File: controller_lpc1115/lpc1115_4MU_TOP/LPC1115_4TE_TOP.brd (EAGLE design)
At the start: 67 x 40.8 mm, 102 parts, among them P2 ISP, Q1 BC856, Q2 BCP52, Q3 BC847C, U1 LPC1115FBD48, U2 BD9G101, U3 XO32 12MHz

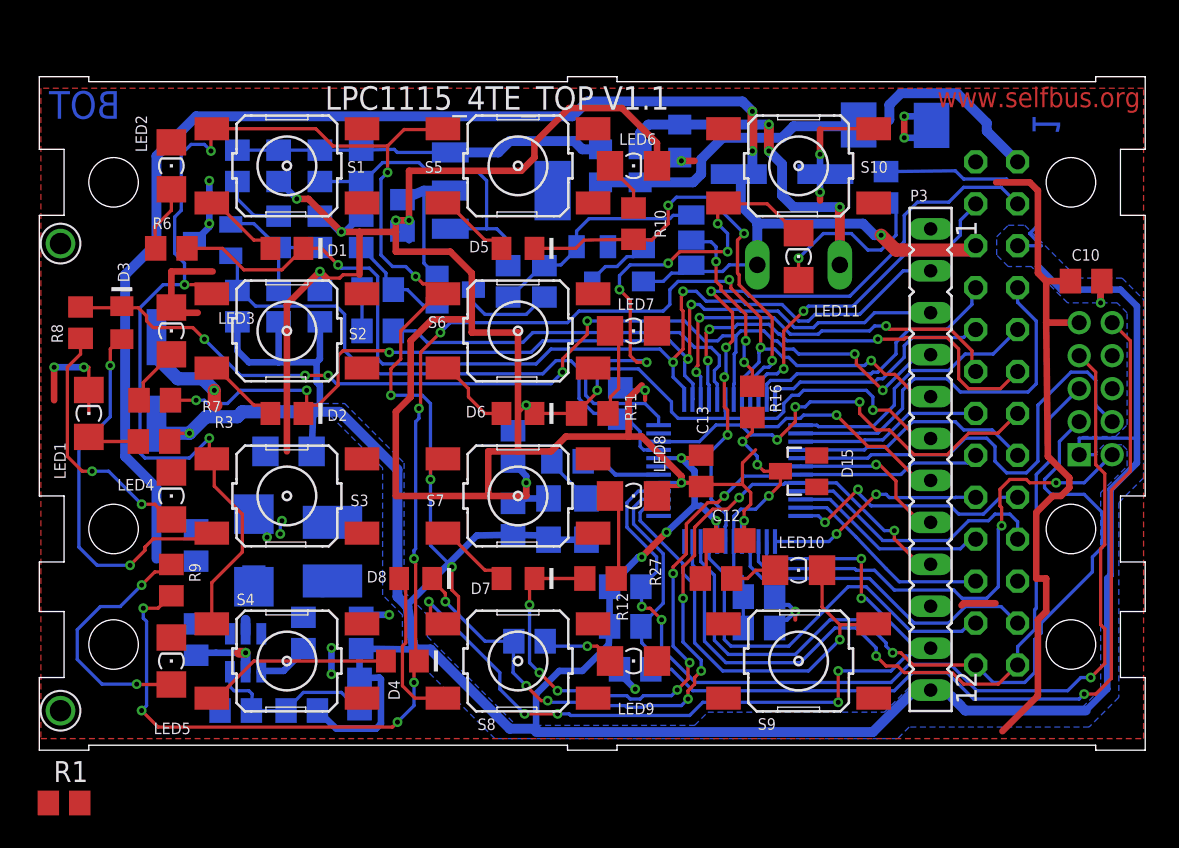
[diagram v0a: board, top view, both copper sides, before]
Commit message: [ctrl_4MU_TOP] - intermediate status of re-routing
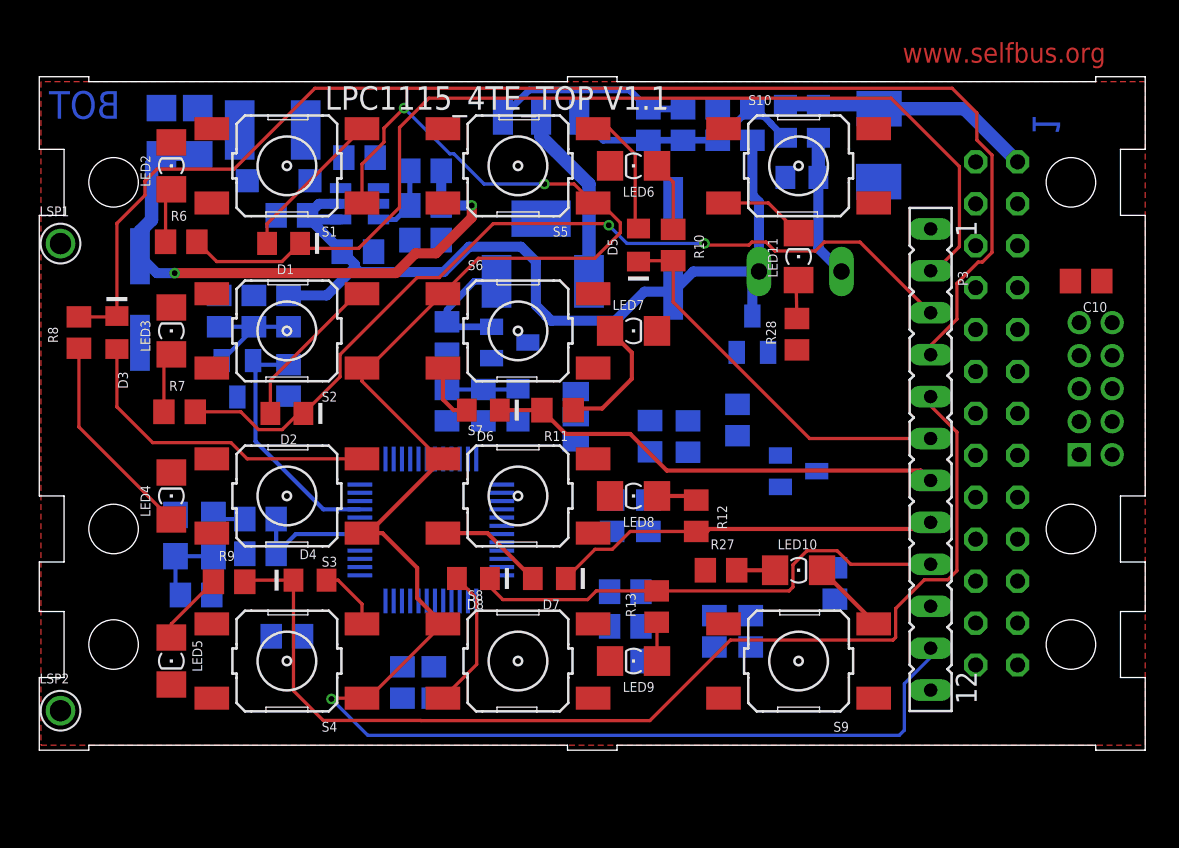
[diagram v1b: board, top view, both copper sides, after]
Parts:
- removed C8: 100nF, rcl:C0805
- removed D10: (*), diode:SMB
- removed LED1: (no value), led:1206
- removed R3: 1k5, rcl:R0805
- added C20: 47uF 10V, rcl:C1206
- added C21: 100nF, rcl:C0805
- C11: value 10n(*) -> 100nF
- C2: value 220n -> 470n
- C6: value 22uF 10V -> 47uF 10V
- D15: value - -> DDZ9685
- L1: value 6.8µH -> 4.7uH; device Stefan_selfbus:1616FPS -> rcl:L4532P
- R1: device rcl:R0805 -> rcl:R2512
- R16: value 36k(*) -> 43k
- R17: value 3k(*) -> 6,2k
- R2: value 2k4 -> 1k6
- R5: value 680R -> 470R
- moved R1 42.9 mm to (30.5, 28.0), flipped to the bottom, turned to 180 degrees
- moved C23 35.4 mm to (48.2, 9.70)
- moved R19 35.0 mm to (40.9, 6.80)
- moved C2 32.0 mm to (23.4, 34.7), turned to 0 degrees
- moved R2 31.5 mm to (23.4, 32.6)
- moved R5 30.7 mm to (23.4, 30.5), turned to 0 degrees
- moved R20 29.4 mm to (43.2, 37.5)
- moved C1 29.0 mm to (19.4, 35.5), turned to 180 degrees
- moved U2 28.1 mm to (19.4, 32.7), turned to 270 degrees
- moved R23 26.7 mm to (41.1, 37.5), turned to 270 degrees
- moved L1 25.8 mm to (14.1, 37.2), turned to 0 degrees
- moved C5 25.5 mm to (19.3, 29.8), turned to 180 degrees
- moved R29 23.0 mm to (34.7, 13.8)
- moved U3 22.6 mm to (9.40, 12.6)
- moved D9 22.2 mm to (14.5, 34.1), turned to 0 degrees
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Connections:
- net N$22 renamed XTALIN
- removed net N$13: LED1.A, R3.2
- removed net N$9: D12.C, D16.3
- new net N$70: D12.C, R24.1, R25.2
- net +3V3: now also C20.1, C21.2, L1.2; no longer C8.1, L1.P$2, R3.1
- net DRAIN: now also R20.1; no longer C14.1
- net EIB_DC: now also C14.1, D16.3, R20.2; no longer D12.A, P1.6
- net EIB_IN: now also C21.1
- net GND: now also C20.2; no longer C8.2, D10.A, LED1.C
- net LX: now also L1.1; no longer D10.C, L1.P$1
- net N$14: now also C14.2; no longer R20.2
- net N$2: now also P1.6; no longer C14.2, R20.1
- net REF: now also D12.A; no longer R24.1, R25.2
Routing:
- net GND: track 243.6 -> 0.00 mm, vias 29 -> 0
- net +3V3: track 205.3 -> 40.5 mm, vias 6 -> 2
- net RESET: track 65.7 -> 0.00 mm, vias 1 -> 0
- net ISP_EN: track 61.9 -> 0.00 mm, vias 3 -> 0
- net IO15: track 49.3 -> 0.00 mm, vias 1 -> 0
- net IO14: track 47.3 -> 0.00 mm, vias 1 -> 0
- net EIB_DC: track 97.3 -> 54.6 mm, vias 3 -> 0
- net PWM: track 39.7 -> 0.00 mm, vias 4 -> 0
- net LT9: track 149.2 -> 115.8 mm, vias 15 -> 3
- net SWDIO: track 30.8 -> 0.00 mm, vias 2 -> 0
- net PROG2: track 33.0 -> 5.31 mm, vias 5 -> 0
- net SWCLK: track 27.4 -> 0.00 mm
- net IO5: track 26.8 -> 0.00 mm, vias 3 -> 0
- net SDA: track 26.5 -> 0.00 mm, vias 3 -> 0
- net IO13: track 24.5 -> 0.00 mm
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- removed copper zone on layer 16, net +3V3
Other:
- board text added: "LPC1115_4TE_TOP V2.0 alpha"
- board text removed: "2"

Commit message: [ctrl_4MU_TOP] - intermediate status of re-routing
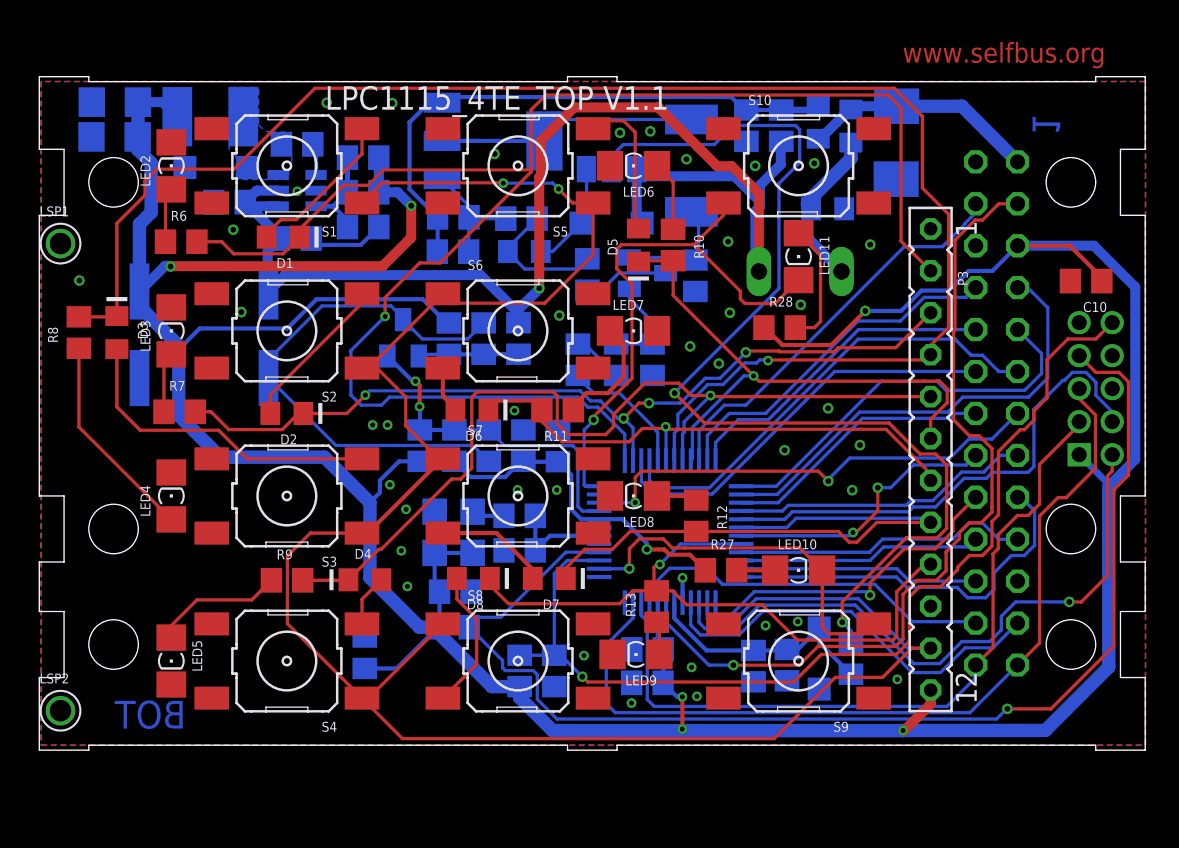
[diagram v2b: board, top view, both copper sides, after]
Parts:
- added C24: 1uF, rcl:C0805
- added C8: 100nF, rcl:C0805
- D15, D16: device diode:SOT23 -> Diode_for_Selfbus-Projects:SOD-123
- moved C23 28.8 mm to (19.7, 5.50)
- moved C3 25.1 mm to (13.9, 24.8), turned to 0 degrees
- moved C17 24.3 mm to (32.6, 23.2), turned to 270 degrees
- moved C11 21.4 mm to (45.3, 4.75)
- moved R17 21.3 mm to (43.3, 4.69)
- moved C21 21.2 mm to (25.1, 18.1)
- moved R19 21.1 mm to (23.1, 18.1)
- moved R16 16.0 mm to (49.2, 5.15)
- moved C18 15.7 mm to (29.1, 13.8)
- moved C22 15.7 mm to (29.1, 11.7)
- moved U3 15.7 mm to (25.1, 12.8)
- moved C19 15.7 mm to (25.2, 9.20)
- moved R30 15.5 mm to (39.8, 28.3)
- moved SJ1 15.2 mm to (34.7, 34.8), turned to 0 degrees
- moved R22 15.0 mm to (25.1, 31.9), turned to 180 degrees
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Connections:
- net +3V3: now also C24.1, C8.1
- net BUS_V: now also D15.C; no longer D15.3
- net EIB_DC: now also D16.C; no longer D16.3
- net GND: now also C24.2, C8.2, D15.A; no longer D15.1
- net N$10: now also Q2.4
- net REF: now also D16.A; no longer D16.1
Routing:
- net +3V3: track 40.5 -> 245.5 mm, vias 2 -> 7
- net ISP_EN: track 0.00 -> 74.1 mm, vias 0 -> 1
- net N$5: track 0.00 -> 65.2 mm, vias 0 -> 2
- net RESET: track 0.00 -> 60.1 mm, vias 0 -> 1
- net IO14: track 0.00 -> 52.5 mm
- net PWM: track 0.00 -> 50.9 mm, vias 0 -> 1
- net IO15: track 0.00 -> 45.3 mm
- net GND: track 0.00 -> 39.6 mm, vias 0 -> 40
- net SWDIO: track 0.00 -> 38.3 mm, vias 0 -> 1
- net LT1: track 62.8 -> 98.7 mm, vias 0 -> 1
- net SWCLK: track 0.00 -> 30.3 mm
- net IO5: track 0.00 -> 29.0 mm, vias 0 -> 2
- net PROG2: track 5.31 -> 33.5 mm, vias 0 -> 1
- net SDA: track 0.00 -> 28.2 mm
- net IO1: track 0.00 -> 28.1 mm
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- added copper zone on layer 16, net GND
- added copper zone on layer 16, net LX

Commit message: [ctrl_4MU_TOP] - v2.0 alpha
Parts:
- removed D9: RB060M-60(*), diode:SOD123
- added C25: 100nF, rcl:C1206
- added D100: RB060M-60(*), diode:SOD123
- C2: value 470n -> 470nF
- C20, C6: device rcl:C1206 -> rcl:C0805
- moved R8 1.37 mm to (3.77, 25.0)
- moved R29 1.29 mm to (37.0, 24.5)
- moved R26 1.28 mm to (34.9, 24.5)
- moved C17 1.28 mm to (32.7, 24.5)
- moved D3 1.24 mm to (5.93, 25.0)
- moved D16 0.85 mm to (34.7, 32.4)
- moved Q3 0.85 mm to (36.9, 29.4)
- moved R25 0.85 mm to (33.2, 29.3)
- moved C4 0.63 mm to (11.0, 32.4)
- moved C10 0.59 mm to (64.0, 28.0)
- moved LED9 0.39 mm to (36.2, 5.01)
- moved LED11 0.16 mm to (46.0, 29.4)
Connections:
- net +3V3: now also C25.1
- net GND: now also C25.2, D100.A; no longer D9.A
- net LX: now also D100.C; no longer D9.C
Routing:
- net SWCLK: track 30.3 -> 24.9 mm
- net PWM: track 50.9 -> 47.6 mm
- net LT4: track 54.1 -> 55.7 mm
- net EIB_OUT: track 8.08 -> 9.33 mm
- net GND: track 39.6 -> 40.2 mm, vias 40 -> 41
- net LT3: track 96.6 -> 96.0 mm
- net N$12: track 6.13 -> 5.58 mm
- net EIB_DC: track 81.6 -> 81.0 mm
- net N$34: track 9.50 -> 8.96 mm
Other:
- board text added: "TOP"
- board text removed: "LPC1115_4TE_TOP V1.1"

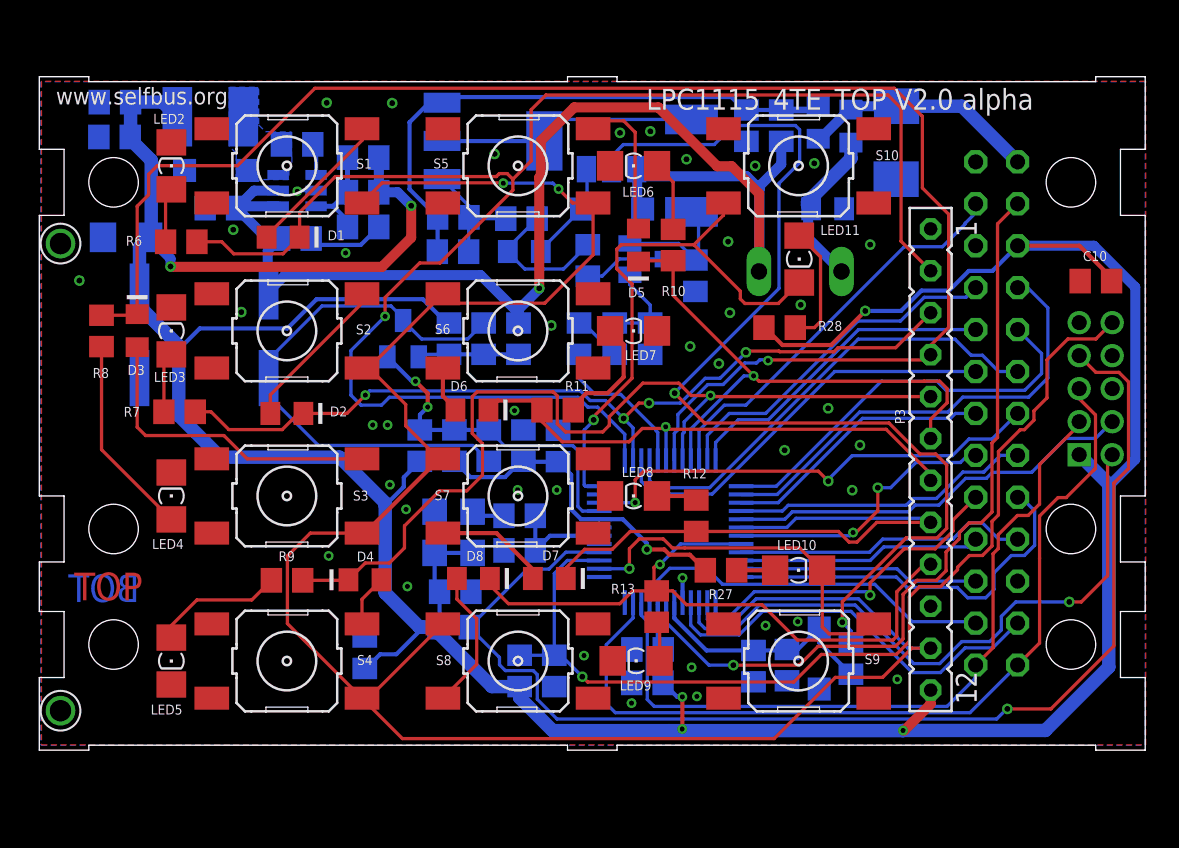
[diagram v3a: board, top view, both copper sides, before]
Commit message: [ctrl_4MU_TOP] - intermediate status of re-routing
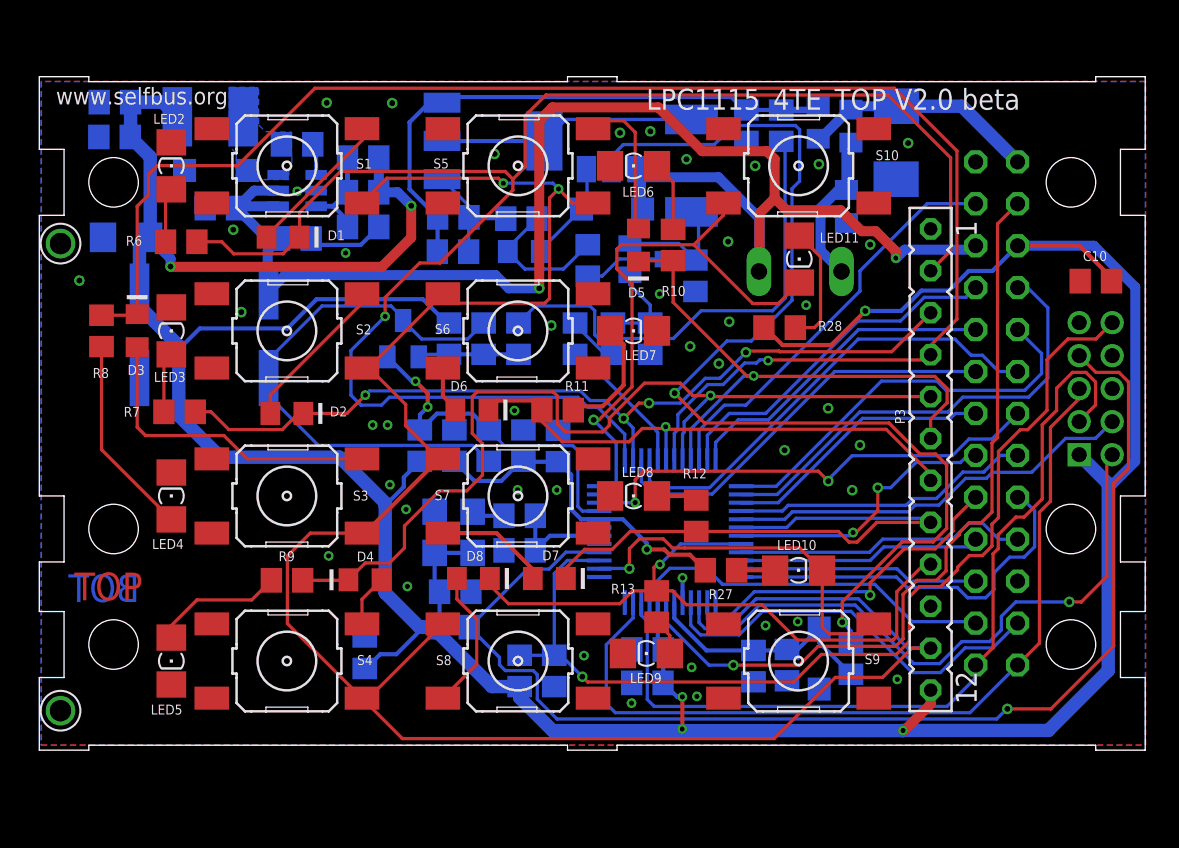
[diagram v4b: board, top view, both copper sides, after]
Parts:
- moved D14 1.15 mm to (48.9, 32.5), turned to 270 degrees
- moved LED9 0.77 mm to (36.8, 5.46)
- moved C17 0.24 mm to (32.5, 24.5)
- moved R26 0.11 mm to (34.8, 24.5)
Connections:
- removed net N$2: P1.6
- new net N$3: C14.1, R20.2
- net EIB_DC: now also P1.6; no longer C14.1, R20.2
- net EIB_IN: no longer C21.1
- net GND: now also C21.1
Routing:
- net N$3: track 0.00 -> 28.9 mm
- net EIB_DC: track 81.0 -> 91.5 mm, vias 1 -> 2
- net IO15: track 45.3 -> 52.5 mm
- net LT1: track 98.3 -> 99.4 mm
- net IO14: track 52.5 -> 51.4 mm
- net N$5: track 65.2 -> 66.0 mm
- net EIB_IN: track 20.7 -> 21.5 mm
- net EIB_OUT: track 9.33 -> 8.71 mm
- net N$8: track 9.90 -> 9.38 mm
- net GND: vias 41 -> 43
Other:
- board text added: "LPC1115_4TE_TOP V2.0 beta"
- board text removed: "LPC1115_4TE_TOP V2.0 alpha"
